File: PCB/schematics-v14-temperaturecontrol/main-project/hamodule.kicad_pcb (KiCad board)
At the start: 2 copper layers, 76.7 x 84.3 mm, 64 parts, among them J1 2604-1104, J10 GND 3.3V, J11 Current Jumper, J2 ESP Relays, J3 2604-1102, J4 2604-1104, J5 Conn_01x02, J6 ESP Sensors, J9 Current Jumper, K1 PCN-105D, K2 PCN-105D, K3 PCN-105D, K4 PCN-105D, U1 ULN2003A, U2 LD1117S33TR_SOT223, U3 HCPL3700, U4 HCPL3700, U5 HCPL3700, U6 HCPL3700

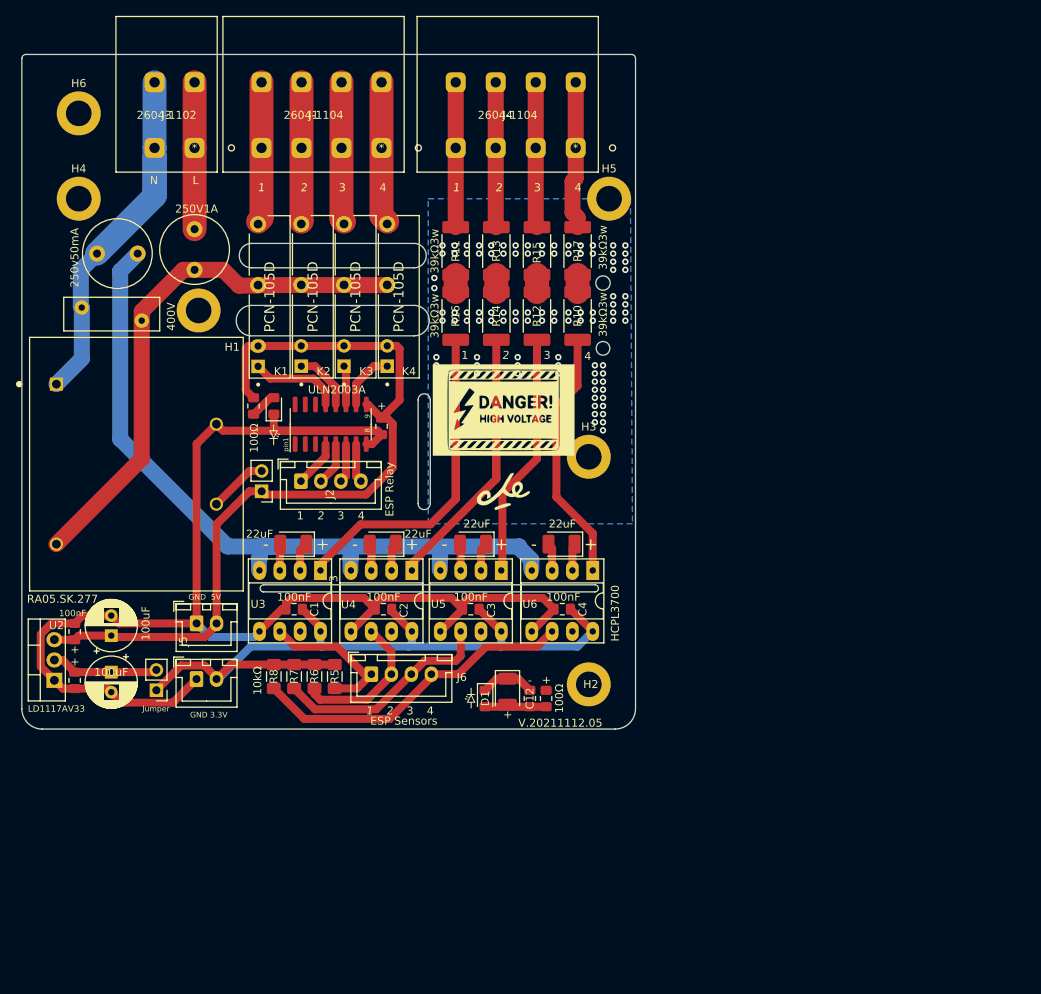
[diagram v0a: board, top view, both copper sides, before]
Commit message: half way with new optocouplers
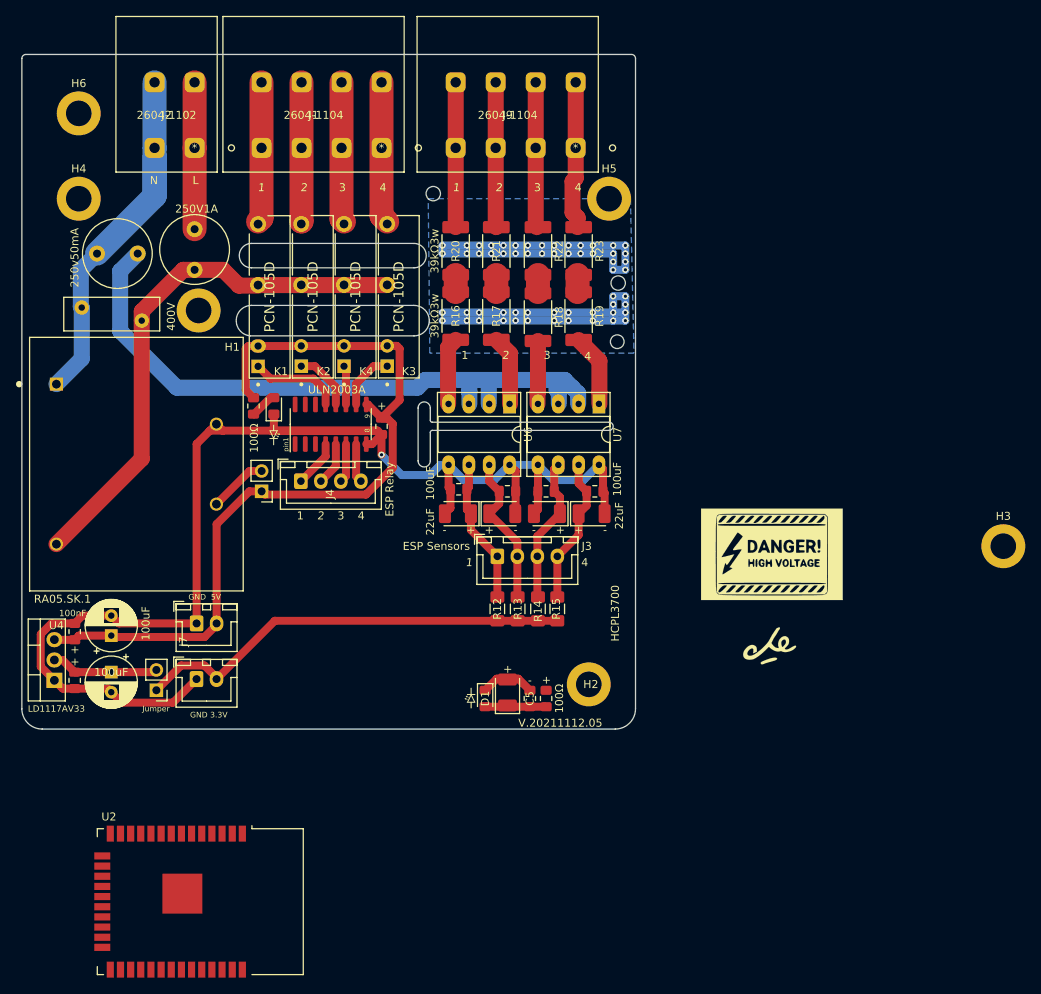
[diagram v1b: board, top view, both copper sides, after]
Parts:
- removed the C1 at (159.2, 136.7)
- removed the C11 at (192.6, 128.6)
- removed the C2 at (170.4, 136.7)
- removed the C3 at (181.3, 136.7)
- removed C4: 100nF, Capacitor_SMD:C_0805_2012Metric_Pad1.15x1.40mm_HandSolder
- removed R10: 39kΩ3w, Resistor_SMD:R_2512_6332Metric_Pad1.52x3.35mm_HandSolder
- removed the R17 at (194.6, 92.0)
- removed R5, R6, R7, R8: 10kΩ, Resistor_SMD:R_1206_3216Metric_Pad1.42x1.75mm_HandSolder
- removed U3, U5: HCPL3700, Package_DIP:DIP-8_W7.62mm_Socket_LongPads
- removed the U4 at (173.9, 131.9)
- added C13: 22uF, Capacitor_Tantalum_SMD:CP_EIA-3528-21_Kemet-B_Pad1.50x2.35mm_HandSolder, F.Cu at (190.8, 124.8)
- added C14: 22uF, Capacitor_Tantalum_SMD:CP_EIA-3528-21_Kemet-B_Pad1.50x2.35mm_HandSolder, F.Cu at (196.4, 124.8)
- added C7: 100uF, Capacitor_SMD:C_0805_2012Metric_Pad1.15x1.40mm_HandSolder, F.Cu at (179.8, 121.7)
- added C8: 100uF, Capacitor_SMD:C_0805_2012Metric_Pad1.15x1.40mm_HandSolder, F.Cu at (185.9, 122.0)
- added C9: 100uF, Capacitor_SMD:C_0805_2012Metric_Pad1.15x1.40mm_HandSolder, F.Cu at (190.7, 122.0)
- added R13: 10kΩ, Resistor_SMD:R_1206_3216Metric_Pad1.42x1.75mm_HandSolder, F.Cu at (187.1, 136.7)
- added R14: 10kΩ, Resistor_SMD:R_1206_3216Metric_Pad1.42x1.75mm_HandSolder, F.Cu at (189.7, 136.7)
- added R18: 39kΩ3w, Resistor_SMD:R_2512_6332Metric_Pad1.52x3.35mm_HandSolder, F.Cu at (189.7, 100.2)
- added R19: 39kΩ3w, Resistor_SMD:R_2512_6332Metric_Pad1.52x3.35mm_HandSolder, F.Cu at (194.8, 100.1)
- added R22: 39kΩ3w, Resistor_SMD:R_2512_6332Metric_Pad1.52x3.35mm_HandSolder, F.Cu at (189.7, 92.0)
- added R23: 39kΩ3w, Resistor_SMD:R_2512_6332Metric_Pad1.52x3.35mm_HandSolder, F.Cu at (194.8, 92.0)
- added U2: ESP32-WROOM-32D, RF_Module:ESP32-WROOM-32, F.Cu at (144.5, 173.3)
- added U7: LDA210-PDIP, Package_DIP:DIP-8_W7.62mm_Socket_LongPads, F.Cu at (197.3, 111.1)
- C10: value 22uF -> 100uF; footprint Capacitor_Tantalum_SMD:CP_EIA-3528-21_Kemet-B_Pad1.50x2.35mm_HandSolder -> Capacitor_SMD:C_0805_2012Metric_Pad1.15x1.40mm_HandSolder
- R12, R15: value 39kΩ3w -> 10kΩ; footprint Resistor_SMD:R_2512_6332Metric_Pad1.52x3.35mm_HandSolder -> Resistor_SMD:R_1206_3216Metric_Pad1.42x1.75mm_HandSolder
- U4: renamed from U2; value LD1117S33TR_SOT223 -> LD1117AV33_TO220
- U6: value HCPL3700 -> LDA210-PDIP
- moved H3 53.0 mm to (247.8, 128.8)
- moved R15 44.8 mm to (192.1, 136.7)
- moved G*** 38.5 mm to (218.6, 141.3)
- moved G*** 38.1 mm to (218.9, 129.9)
- moved R12 37.0 mm to (184.6, 136.7), turned to 90 degrees
- moved U6 23.3 mm to (186.1, 111.1)
- moved J3 21.6 mm to (184.6, 130.1)
- moved C11 20.9 mm to (179.7, 124.8)
- moved C10 16.6 mm to (196.8, 122.0), turned to 0 degrees
- moved C12 15.4 mm to (185.2, 124.8), turned to 0 degrees
- moved C6 0.10 mm to (185.9, 147.1), turned to 90 degrees
- renumbered C6 to C1, C8 to C11, C9 to C12, C7 to C2, C5 to C3, C12 to C5, C13 to C6, D9 to D2, J3 to J2, J6 to J3, J2 to J4, J11 to J5, J10 to J6, J5 to J7, J9 to J8, J4 to J9, K4 to K3, K3 to K4, R9 to R11, R14 to R17, R11 to R20, R13 to R21, R1 to R9, RA05.SK.277 to RA05.SK.1
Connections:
- C10 pad 1: Net-(C10-Pad1) -> EspSens4
- C10 pad 2: Net-(C10-Pad2) -> GND(5V)
- C11 pad 1: Net-(C8-Pad1) -> EspSens1
- C11 pad 2: Net-(C8-Pad2) -> GND(5V)
- C12 pad 1: Net-(C9-Pad1) -> EspSens2
- C12 pad 2: Net-(C9-Pad2) -> GND(5V)
- C5 pad 1: Net-(C12-Pad1) -> Net-(C5-Pad1)
- C5 pad 2: Net-(C12-Pad2) -> Net-(C5-Pad2)
- C6 pad 1: Net-(C12-Pad2) -> Net-(C5-Pad1)
- C6 pad 2: Net-(C12-Pad1) -> Net-(C5-Pad2)
- D1 pad 1: Net-(C12-Pad2) -> Net-(C5-Pad2)
- D1 pad 2: Net-(C12-Pad1) -> Net-(C5-Pad1)
- J3 pad 1: EspSens4 -> EspSens1
- J3 pad 2: EspSens3 -> EspSens2
- J3 pad 3: EspSens2 -> EspSens3
- J3 pad 4: EspSens1 -> EspSens4
- R12 pad 1: Net-(R12-Pad1) -> 3.3V+
- R12 pad 2: Net-(R12-Pad2) -> EspSens1
- R15 pad 1: Sens3 -> EspSens4
- R15 pad 2: Net-(R12-Pad1) -> 3.3V+
- R17 pad 2: Net-(R14-Pad2) -> Net-(R17-Pad2)
- R9 pad 1: Net-(C12-Pad1) -> Net-(C5-Pad1)
- U6 pad 1: Net-(R10-Pad2) -> Net-(R17-Pad2)
- U6 pad 2: Net-(C11-Pad1) -> 220VAC(N)
- U6 pad 3: Net-(C11-Pad2) -> 220VAC(N)
- U6 pad 4: 220VAC(N) -> Net-(R16-Pad2)
- U6 pad 7: (no net) -> EspSens2
- U6 pad 8: 3.3V+ -> GND(5V)
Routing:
- net (no net): track 0.00 -> 105.2 mm, vias 99 -> 58
- net Net-(R16-Pad2): track 54.3 -> 8.41 mm
- net Net-(R14-Pad2): track 44.1 -> 0.00 mm
- net 3.3V+: track 96.0 -> 55.2 mm
- net Net-(R10-Pad2): track 31.8 -> 0.00 mm
- net Net-(R12-Pad2): track 31.3 -> 0.00 mm
- net EspSens1: track 41.1 -> 18.2 mm
- net 220VAC(N): track 94.3 -> 82.3 mm
- net Net-(R19-Pad2): track 0.00 -> 9.07 mm
- net Net-(R17-Pad2): track 0.00 -> 8.72 mm
- net EspSens2: track 27.7 -> 19.0 mm
- net Net-(R18-Pad2): track 0.00 -> 8.53 mm
- net Net-(C5-Pad1): track 0.00 -> 7.62 mm
- net Net-(C12-Pad1): track 7.62 -> 0.00 mm
- net Net-(C5-Pad2): track 0.00 -> 6.79 mm
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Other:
- outline, holes or cut-outs redrawn
- board text removed: "+"
- board text removed: "-"

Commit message: removing vias
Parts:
- removed H3: MountingHole_Pad, MountingHole:MountingHole_3.2mm_M3_ISO14580_Pad
- removed U2: ESP32-WROOM-32D, RF_Module:ESP32-WROOM-32
- moved G*** 51.2 mm to (168.1, 136.2)
- moved G*** 51.0 mm to (167.8, 145.6)
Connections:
- H5 pad 1: (no net) -> Net-(H5-Pad1)
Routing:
- net (no net): track 105.2 -> 0.00 mm, vias 58 -> 0
- added copper zone on B.Cu, net Net-(H5-Pad1)
- removed copper zone on B.Cu, net (none)
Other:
- outline, holes or cut-outs redrawn
